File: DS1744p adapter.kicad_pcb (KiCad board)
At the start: 2 copper layers, 34 x 47.2 mm, 4 parts, among them P1 DS1742W, U1 DS1744P

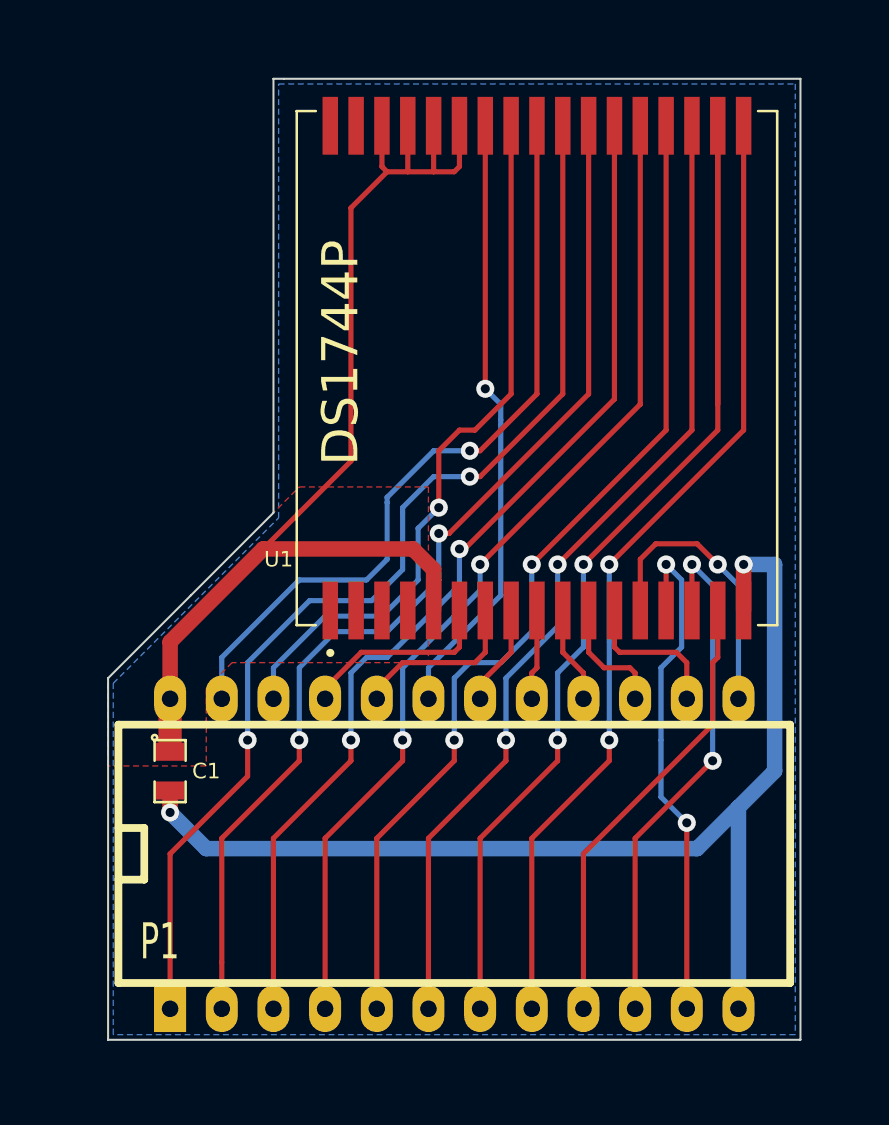
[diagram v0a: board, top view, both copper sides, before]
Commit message: cleaned up and updated for KiCAD 7
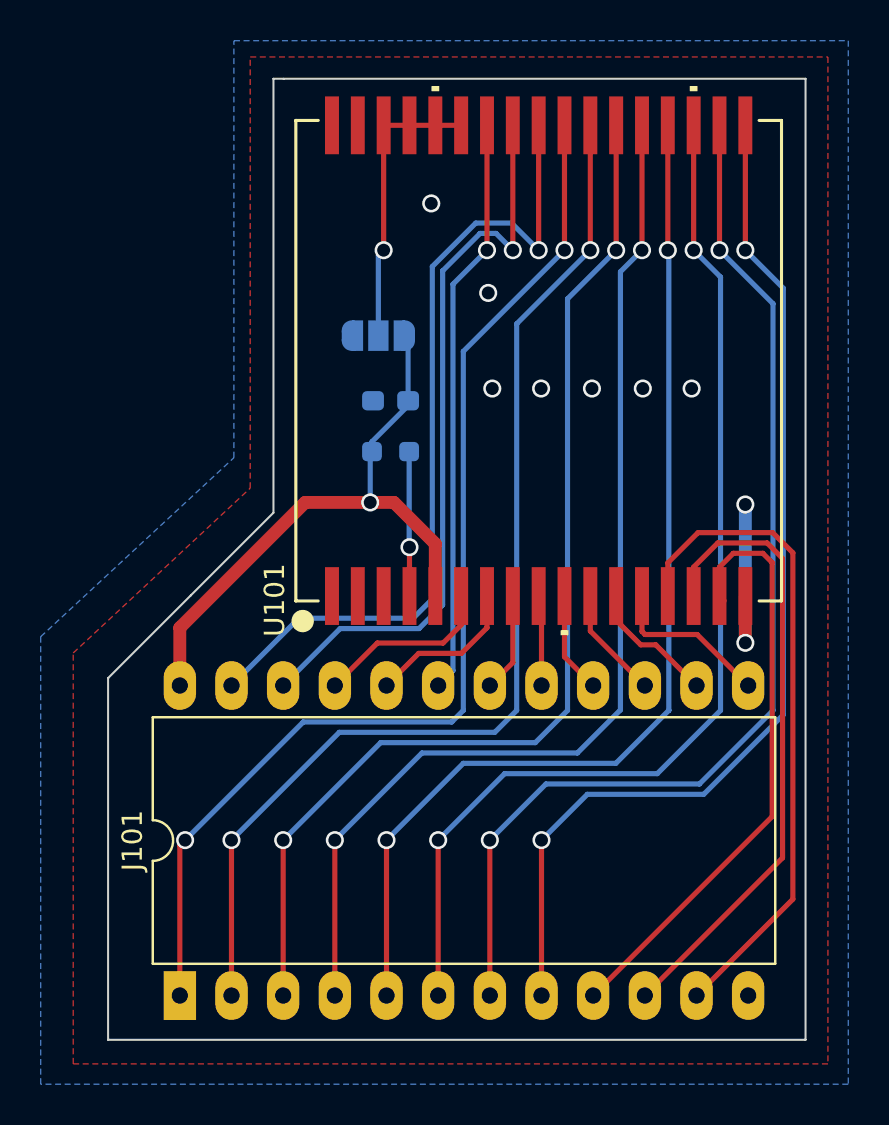
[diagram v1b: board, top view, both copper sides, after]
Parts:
- removed C1: 100n, SM0805
- removed P1: DS1742W, DIP-24__600_ELL
- removed U1: DS1744P, DALLAS_DS1554P-70+
- removed VAL: REF, cat_300
- added C101: 100n, Capacitor_SMD:C_0603_1608Metric_Pad1.08x0.95mm_HandSolder, B.Cu at (202.1, 147.4)
- added J101: DS1742W, DS1744p-adapter:DIP-24_W15.24mm_LongPads, F.Cu at (191.7, 176.6)
- added JP101: ~, Jumper:SolderJumper-3_P1.3mm_Open_RoundedPad1.0x1.5mm, B.Cu at (201.5, 144.2)
- added R101: 10k, Resistor_SMD:R_0603_1608Metric_Pad0.98x0.95mm_HandSolder, B.Cu at (202.1, 149.9)
- added U101: ds1744p-70+, DS1744p-adapter:21-0246_PC2&plus_2_MXM, F.Cu at (209.4, 145.4)
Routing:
- net +3.3V: track 56.3 -> 0.00 mm
- net GND: track 57.0 -> 9.10 mm, vias 2 -> 9
- net +3V3: track 0.00 -> 30.5 mm, vias 0 -> 1
- net Net-(JP101-C): track 0.00 -> 14.3 mm, vias 0 -> 1
- net /~WE: track 9.76 -> 0.00 mm
- net /*WE: track 0.00 -> 8.87 mm
- net /~OE: track 8.64 -> 0.00 mm
- net /A1: track 61.9 -> 54.1 mm
- net /*OE: track 0.00 -> 7.68 mm
- net /DQ0: track 22.3 -> 29.8 mm
- net /DQ2: track 25.4 -> 32.5 mm, vias 2 -> 0
- net Net-(U101-*RST): track 0.00 -> 7.11 mm, vias 0 -> 1
- net /DQ3: track 14.1 -> 8.06 mm, vias 1 -> 0
- net /~CE: track 4.97 -> 0.00 mm
- net /*CE: track 0.00 -> 4.87 mm
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- added copper zone on F.Cu, net GND
- removed copper zone on F.Cu, net +3.3V
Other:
- board size 34 x 47.2 mm -> 34.3 x 47.2 mm
- net class Default removed
- board text added: "Install date"
